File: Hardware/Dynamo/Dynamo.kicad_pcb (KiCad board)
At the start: 2 copper layers, 69.2 x 53.9 mm, 44 parts, among them U1 AP63205WU, U10 ESP32-S3-WROOM-1, U11 NCP1117-3.3_SOT223, U13 TXS0102DCT, U14 TXS0102DCT, U2 TLP2770, U3 TLP2770, U4 74LVC1G86, U5 74LVC1G86, U6 74LVC1G86, U7 74LVC1G86, U8 74LVC1G86, U9 74LVC1G86

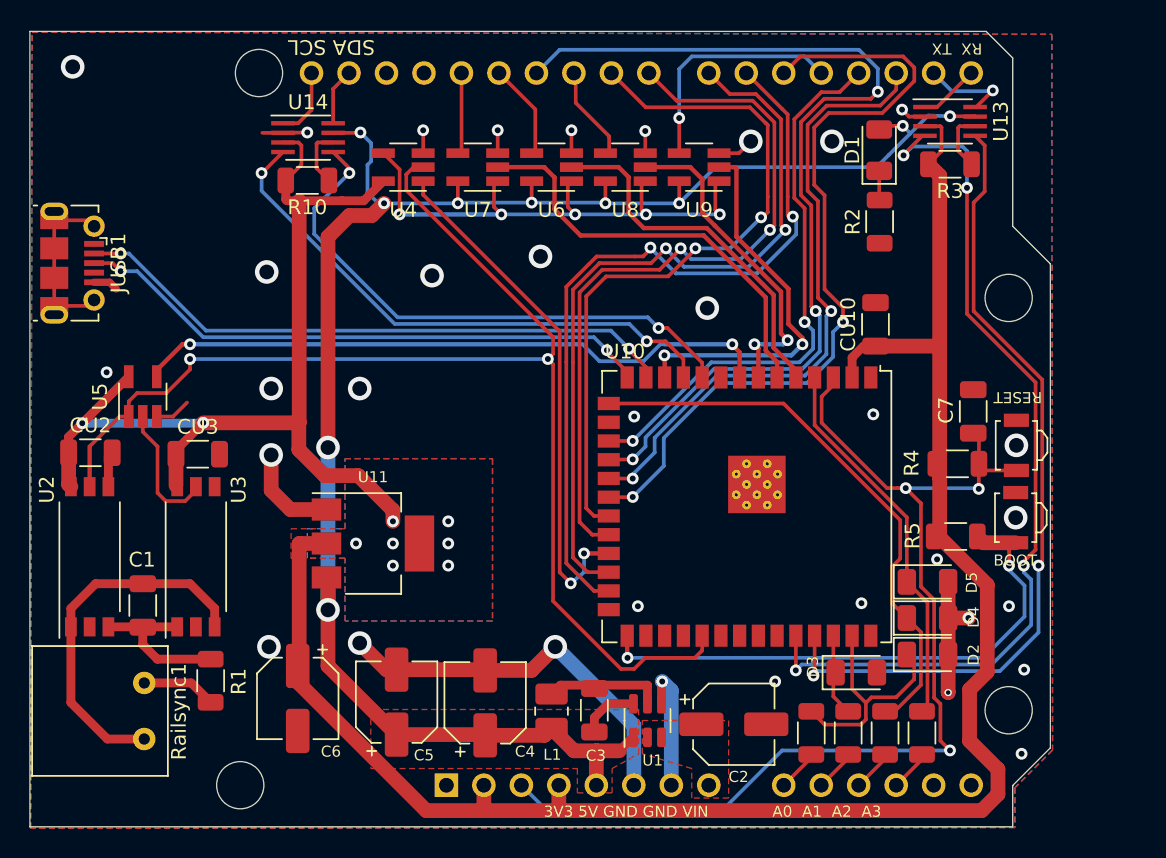
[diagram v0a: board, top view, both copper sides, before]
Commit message: Completed BOM, minor changes to schematic and PCB
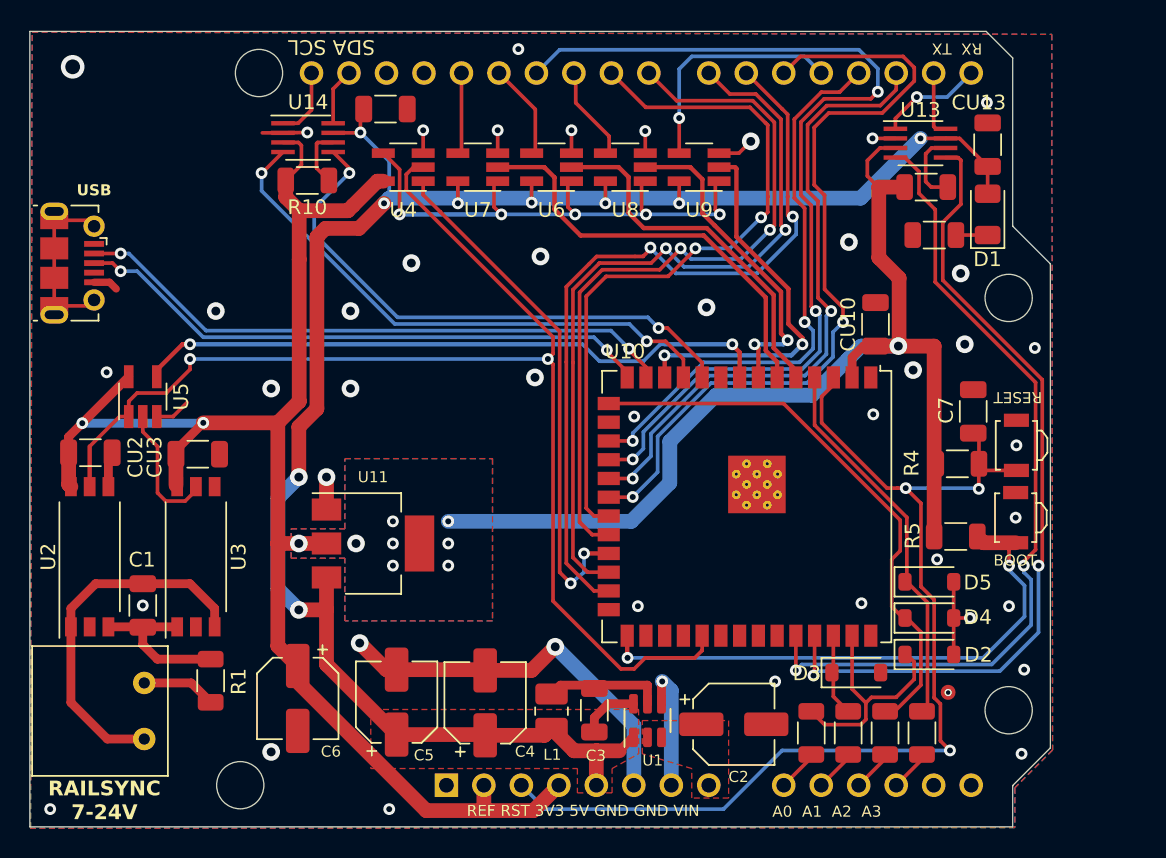
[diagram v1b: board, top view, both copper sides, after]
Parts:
- added CU13: 0.1uF, Capacitor_SMD:C_1206_3216Metric, F.Cu at (186.6, 56.5)
- added CU14: 0.1uF, Capacitor_SMD:C_1206_3216Metric, F.Cu at (145.7, 54.1)
- C1: value 10pf -> 330pf
- D2, D3, D4, D5: footprint Diode_SMD:D_1206_3216Metric -> Diode_SMD:D_SOD-123
- moved D1 8.54 mm to (186.6, 61.2)
- moved R2 3.82 mm to (182.9, 62.6), turned to 0 degrees
- moved U13 2.49 mm to (182.0, 56.4)
- moved R3 2.24 mm to (182.4, 59.4)
- moved D2 0.12 mm to (182.6, 91.0)
- moved D4 0.12 mm to (182.6, 88.5)
- moved D5 0.12 mm to (182.6, 86.1)
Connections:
- net /PWM1 renamed /ENA_1
- net /PWM2 renamed /ENA_2
- net /PWM3 renamed /ENA_3
- net /PWM4 renamed /ENA_4
- JUSB1 pad 6: unconnected-(JUSB1-Shield-Pad6) -> GND
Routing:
- net +3.3V: track 191.8 -> 174.2 mm, vias 9 -> 11
- net unconnected-(JUSB1-Shield-Pad6): track 12.7 -> 0.00 mm
- net +5V: track 120.9 -> 126.7 mm, vias 10 -> 9
- net GND: track 71.4 -> 76.5 mm, vias 34 -> 45
- net Net-(U10-U0RXD/GPIO44/CLK_OUT2): track 60.8 -> 56.1 mm, vias 4 -> 2
- net /RXD: track 4.09 -> 7.11 mm, vias 0 -> 1
- net /TXD: track 6.31 -> 4.49 mm, vias 1 -> 0
- net Net-(U13-OE): track 4.04 -> 5.05 mm
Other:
- board text added: "Dynamo DCC Booster"
- board text added: "RAILSYNC 7-24V"
- board text added: "REF RST 3V3 5V GND GND VIN"
- board text added: "Seraphimlabs LLC 2023 github.com/SeraphimlabsLLC"
- board text added: "USB"
- board text removed: "3V3 5V GND GND VIN"

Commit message: Revised L1 for possible 2A output, cleaner fill zones, fabrication outputs
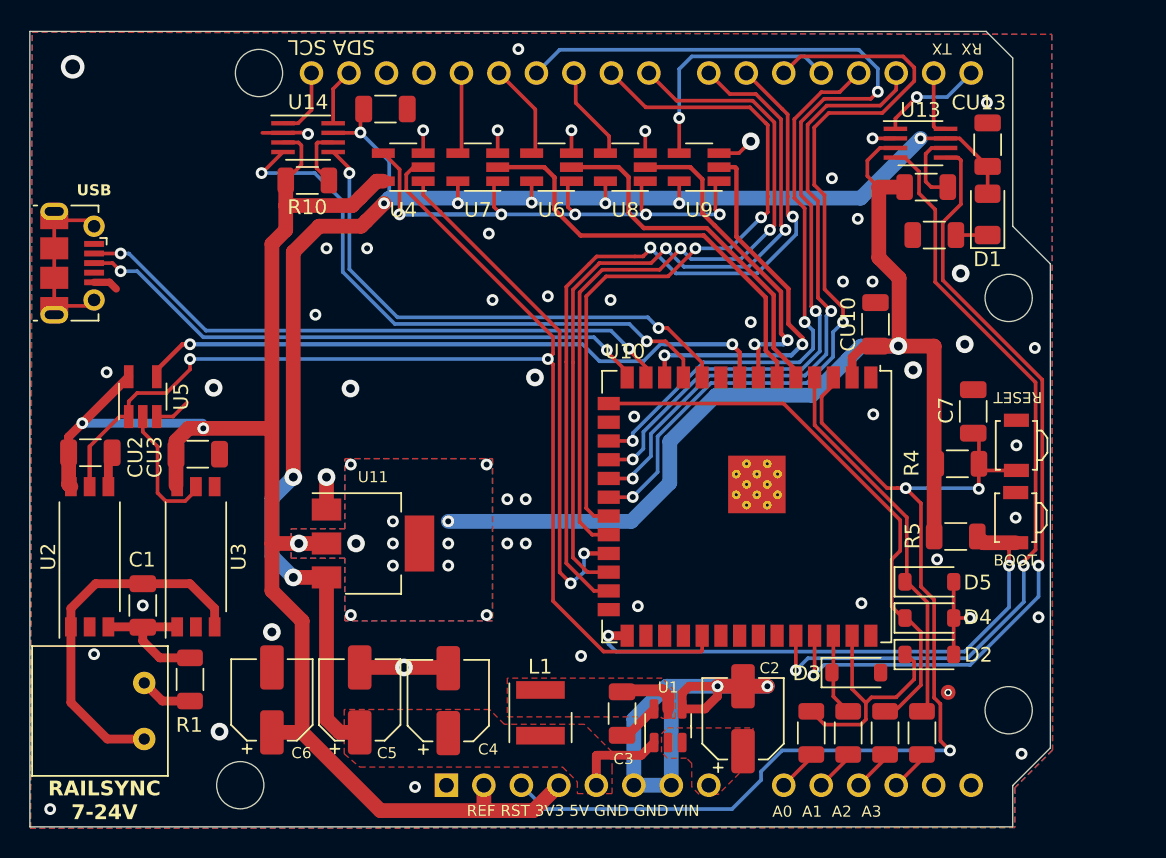
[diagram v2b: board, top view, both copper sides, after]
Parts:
- L1: footprint Inductor_SMD:L_1008_2520Metric_Pad1.43x2.20mm_HandSolder -> Inductor_SMD_Wurth:L_Wurth_WE-LQSH-4020
- moved C5 2.50 mm to (144.0, 94.1)
- moved C4 2.50 mm to (150.0, 94.2)
- moved C3 1.89 mm to (161.8, 95.0)
- moved C6 1.75 mm to (138.1, 94.1), turned to 90 degrees
- moved U1 1.44 mm to (164.9, 95.8)
- moved R1 1.40 mm to (132.5, 92.7)
- moved L1 0.76 mm to (156.2, 95.0)
- moved C2 0.73 mm to (170.0, 95.4), turned to 90 degrees
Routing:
- net +5V: track 126.7 -> 111.3 mm
- net +3.3V: track 174.2 -> 179.9 mm, vias 11 -> 15
- net GND: track 76.5 -> 81.8 mm, vias 45 -> 56
- net Net-(U1-SW): track 8.01 -> 4.06 mm
- net /SCL: track 37.8 -> 39.9 mm
- net /SDA: track 37.9 -> 35.9 mm
- net Net-(U10-U0RXD/GPIO44/CLK_OUT2): track 56.1 -> 54.5 mm
- net Net-(U2-K): track 10.9 -> 9.28 mm
- net /RAILSYNC_A: track 5.04 -> 3.61 mm
- net Net-(U10-U0TXD/GPIO43/CLK_OUT1): track 55.7 -> 54.3 mm
- net Net-(U1-BST): track 4.01 -> 2.92 mm
- net /DIR_MONITOR: track 85.4 -> 84.5 mm
- added copper zone on F.Cu, net Net-(U1-SW)

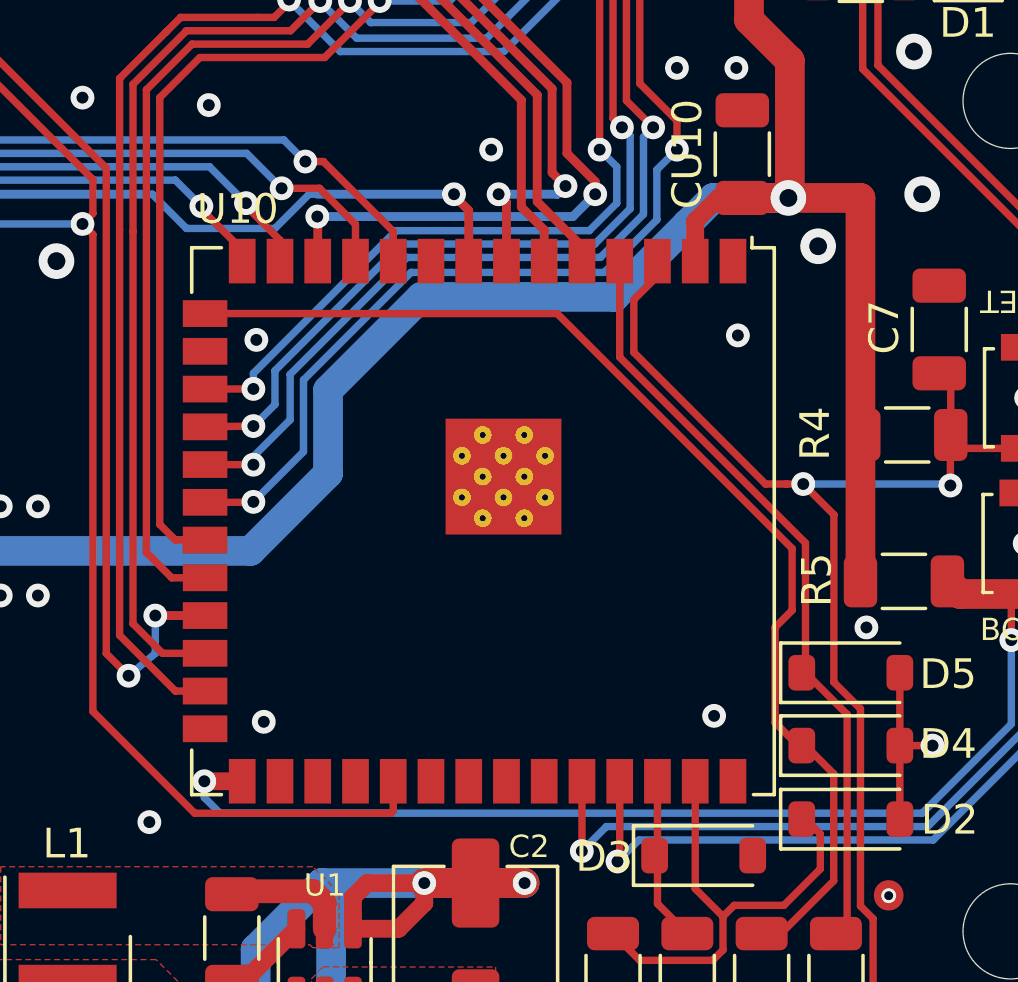
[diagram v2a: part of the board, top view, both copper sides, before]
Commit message: TrackChannel struct + extern in main working, MAX_TRACKS not accessible in main
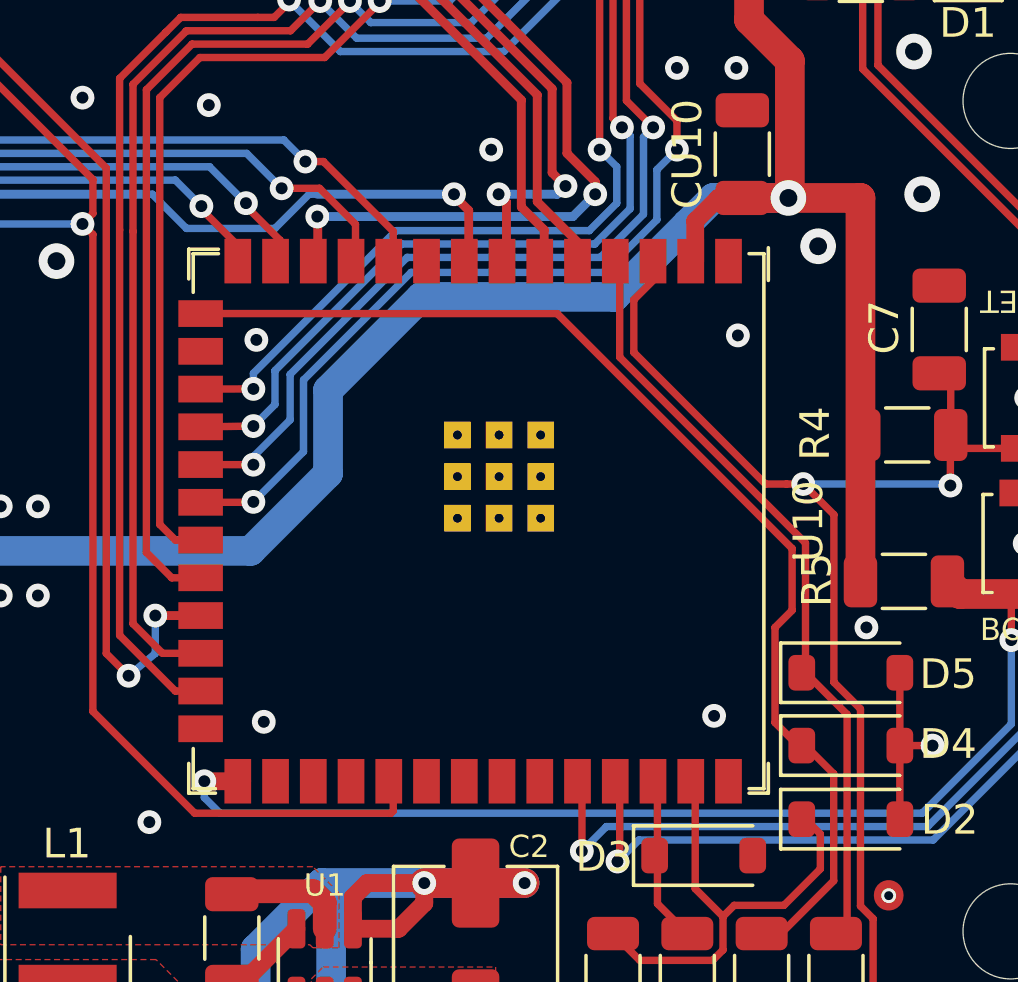
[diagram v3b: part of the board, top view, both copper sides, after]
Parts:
- Railsync1: value screw_terminal -> WR-TBL 2P
- U10: footprint RF_Module:ESP32-S3-WROOM-1U -> Espressif:ESP32-S3-WROOM-1U

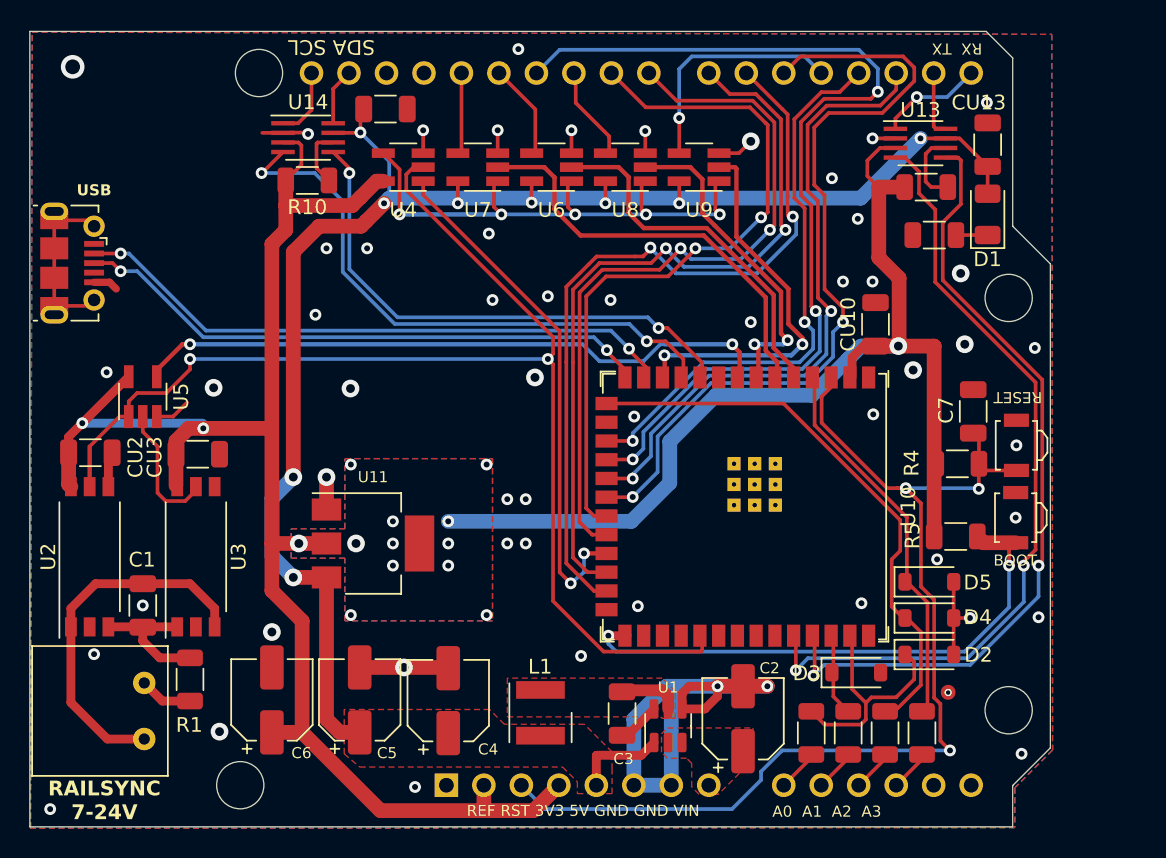
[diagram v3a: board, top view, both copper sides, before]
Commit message: Schematic features changed: Added USB power for programming, per-track DC mode gating. New PCB layout improving on previous builds.
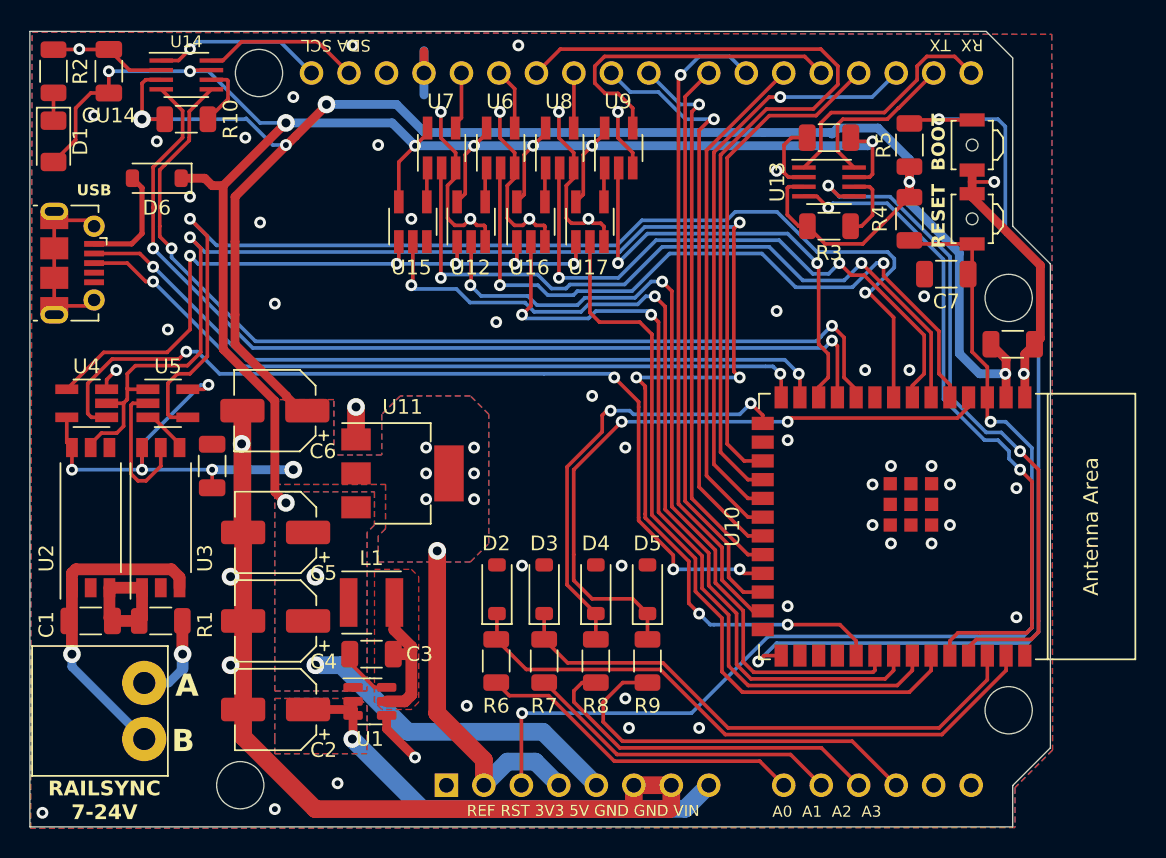
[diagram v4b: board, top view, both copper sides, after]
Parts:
- removed CU3: 0.1uF, Capacitor_SMD:C_1206_3216Metric
- added D6: PMEG2005EGWX, Diode_SMD:D_SOD-123, F.Cu at (130.2, 58.8)
- added U12: 74AHC1G32, Package_TO_SOT_SMD:SOT-23-5_HandSoldering, F.Cu at (151.6, 61.7)
- added U15: 74AHC1G32, Package_TO_SOT_SMD:SOT-23-5_HandSoldering, F.Cu at (147.6, 61.7)
- added U16: 74AHC1G32, Package_TO_SOT_SMD:SOT-23-5_HandSoldering, F.Cu at (155.6, 61.7)
- added U17: 74AHC1G32, Package_TO_SOT_SMD:SOT-23-5_HandSoldering, F.Cu at (159.6, 61.7)
- BOOT1, RESET1: footprint Button_Switch_SMD:SW_SPST_B3U-3000P -> Button_Switch_SMD:SW_SPST_B3U-3000P-B
- U10: footprint Espressif:ESP32-S3-WROOM-1U -> Espressif:ESP32-S3-WROOM-1
- moved D1 63.5 mm to (123.2, 56.2), turned to -90 degrees
- moved R2 60.7 mm to (123.2, 51.5), turned to -90 degrees
- moved C2 31.7 mm to (138.3, 94.8), turned to 180 degrees
- moved D2 29.6 mm to (153.3, 86.6), turned to 90 degrees
- moved U4 26.8 mm to (125.5, 74.0)
- moved R5 26.7 mm to (181.2, 56.5), turned to -90 degrees
- moved BOOT1 25.4 mm to (185.5, 56.5)
- moved D4 22.7 mm to (160.0, 86.6), turned to 90 degrees
- moved R6 21.9 mm to (153.2, 91.5)
- moved D3 21.9 mm to (156.5, 86.6), turned to 90 degrees
- moved R7 21.2 mm to (156.5, 91.5)
- moved U1 20.3 mm to (144.7, 94.2), turned to 0 degrees
- moved R8 20.2 mm to (160.0, 91.5)
- moved C6 19.6 mm to (138.2, 74.5), turned to 180 degrees
- moved R9 19.2 mm to (163.5, 91.5)
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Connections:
- BOOT1 pad 1: GND -> /BOOT
- BOOT1 pad 2: /BOOT -> GND
- JUSB1 pad 1: unconnected-(JUSB1-VBUS-Pad1) -> Net-(D6-A)
- U10 pad 32: unconnected-(U10-MTCK/GPIO39/CLK_OUT3/SUBSPICS1-Pad32) -> /DC_1
- U10 pad 33: unconnected-(U10-MTDO/GPIO40/CLK_OUT2-Pad33) -> /DC_2
- U10 pad 34: unconnected-(U10-MTDI/GPIO41/CLK_OUT1-Pad34) -> /DC_3
- U10 pad 35: unconnected-(U10-MTMS/GPIO42-Pad35) -> /DC_4
- U6 pad 1: /DIR -> Net-(U12-Pad4)
- U7 pad 1: /DIR -> Net-(U15-Pad4)
- U8 pad 1: /DIR -> Net-(U16-Pad4)
- U9 pad 1: /DIR -> Net-(U17-Pad4)
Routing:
- net GND: track 81.8 -> 160.4 mm, vias 56 -> 57
- net /DC_2: track 0.00 -> 60.2 mm, vias 0 -> 2
- net /DC_1: track 0.00 -> 55.6 mm, vias 0 -> 2
- net /DC_3: track 0.00 -> 54.8 mm, vias 0 -> 2
- net /DC_4: track 0.00 -> 50.8 mm
- net /MASTER_EN: track 43.7 -> 78.8 mm
- net +5V: track 111.3 -> 145.6 mm, vias 9 -> 11
- net VIN: track 0.00 -> 32.4 mm, vias 0 -> 1
- net /A1p: track 5.54 -> 37.3 mm
- net /SDA: track 35.9 -> 66.3 mm
- net /BOOT: track 37.8 -> 65.9 mm
- net /DIR_OVERRIDE: track 35.5 -> 61.6 mm, vias 2 -> 4
- net /A0p: track 16.1 -> 41.8 mm
- net /SCL: track 39.9 -> 65.2 mm
- net /DIR_MONITOR: track 84.5 -> 109.4 mm, vias 2 -> 6
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- added copper zone on B.Cu, net +5V
- added copper zone on B.Cu, net VIN
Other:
- board text added: "A"
- board text added: "B"

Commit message: Final cleanup, added tags for JLCPCB Fabrication
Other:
- board text added: "JLCJLCJLCJLC"
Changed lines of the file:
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@@
   (gr_line (start 121.65 48.8) (end 186.45 48.8)
     (stroke (width 0.05) (type solid)) (layer "Edge.Cuts"))
-  (gr_text "Seraphimlabs LLC 2023\ngithub.com/SeraphimlabsLLC" (at 147.525 74.2) (layer "B.SilkS")
+  (gr_text "Seraphimlabs LLC 2023\ngithub.com/SeraphimlabsLLC" (at 156.95 79.9) (layer "B.SilkS")
     (effects (font (size 1.2 1.2) (thickness 0.15) bold) (justify bottom mirror))
   )
-  (gr_text "Dynamo\nDCC Booster" (at 146.975 70.45) (layer "B.SilkS")
+  (gr_text "JLCJLCJLCJLC" (at 190.2 77 90) (layer "B.SilkS")
+    (effects (font (size 1 1) (thickness 0.2) bold) (justify left bottom mirror))
+  )
+  (gr_text "Dynamo\nDCC Booster" (at 156.4 76.15) (layer "B.SilkS")
     (effects (font (size 3 3) (thickness 0.6) bold) (justify bottom mirror))
   )
